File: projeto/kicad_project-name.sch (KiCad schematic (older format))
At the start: 26 parts, among them J1 USB_C_Receptacle_USB2.0, J2 Conn_01x04_Female, Q1 MMBT3904, Q2 MMBT3904, SW1 SW_Push, SW2 SW_Push, U1 TLV75733PDBV, U2 CH340G, U3 ESP32-WROOM-32D, Y1 12MHz 10ppm

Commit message: Troca do LDO para AMS1117-3-3
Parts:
- removed R1: 10kR, Resistor_SMD:R_0603_1608Metric, symbol Device:R_US
- removed SW2: SW_Push, Switches:TACTILE_SWITCH_SMD_6.0X3.5MM, symbol Switch:SW_Push
- removed U1: TLV75733PDBV, Package_TO_SOT_SMD:SOT-23-5, symbol Regulator_Linear:TLV75733PDBV
- added C? (x4): 100nF, Capacitor_SMD:C_0603_1608Metric, symbol Device:C_Small
- added C?: 10nF, Capacitor_SMD:C_0603_1608Metric, symbol Device:C_Small
- added C?: 10uF, Capacitor_Tantalum_SMD:CP_EIA-3216-12_Kemet-S, symbol Device:CP1_Small
- added J?: JTAG 10pin Connector, Connector_PinHeader_1.27mm:PinHeader_2x05_P1.27mm_Vertical_SMD, symbol Connector:Conn_ARM_JTAG_SWD_10
- added R? (x2): 10kR, Resistor_SMD:R_0603_1608Metric, symbol Device:R_US
- added R? (x2): 5k1R, Resistor_SMD:R_0603_1608Metric, symbol Device:R_US
- added SW?: SW_Push, Switches:TACTILE_SWITCH_SMD_6.0X3.5MM, symbol Switch:SW_Push
- added U?: AMS1117-3.3, Package_TO_SOT_SMD:SOT-223-3_TabPin2, symbol Regulator_Linear:AMS1117-3.3
- C7, C8: value C_Small -> 100nF
- J2: value Conn_01x04_Female -> OLED
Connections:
- net labels added: JTAG_RST, MTCK, MTDI, MTDO, MTMS
- net labels removed: 3V3_EN
- wire segments 89 -> 143
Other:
- note added: "Conector Debug/JTAG"
- note added: "OLED"
- note added: "Reset e Boot"
- moved on the sheet: C1, C2, C3, C4, C5, C6, C7, C8, D1, J1, J2, Q1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

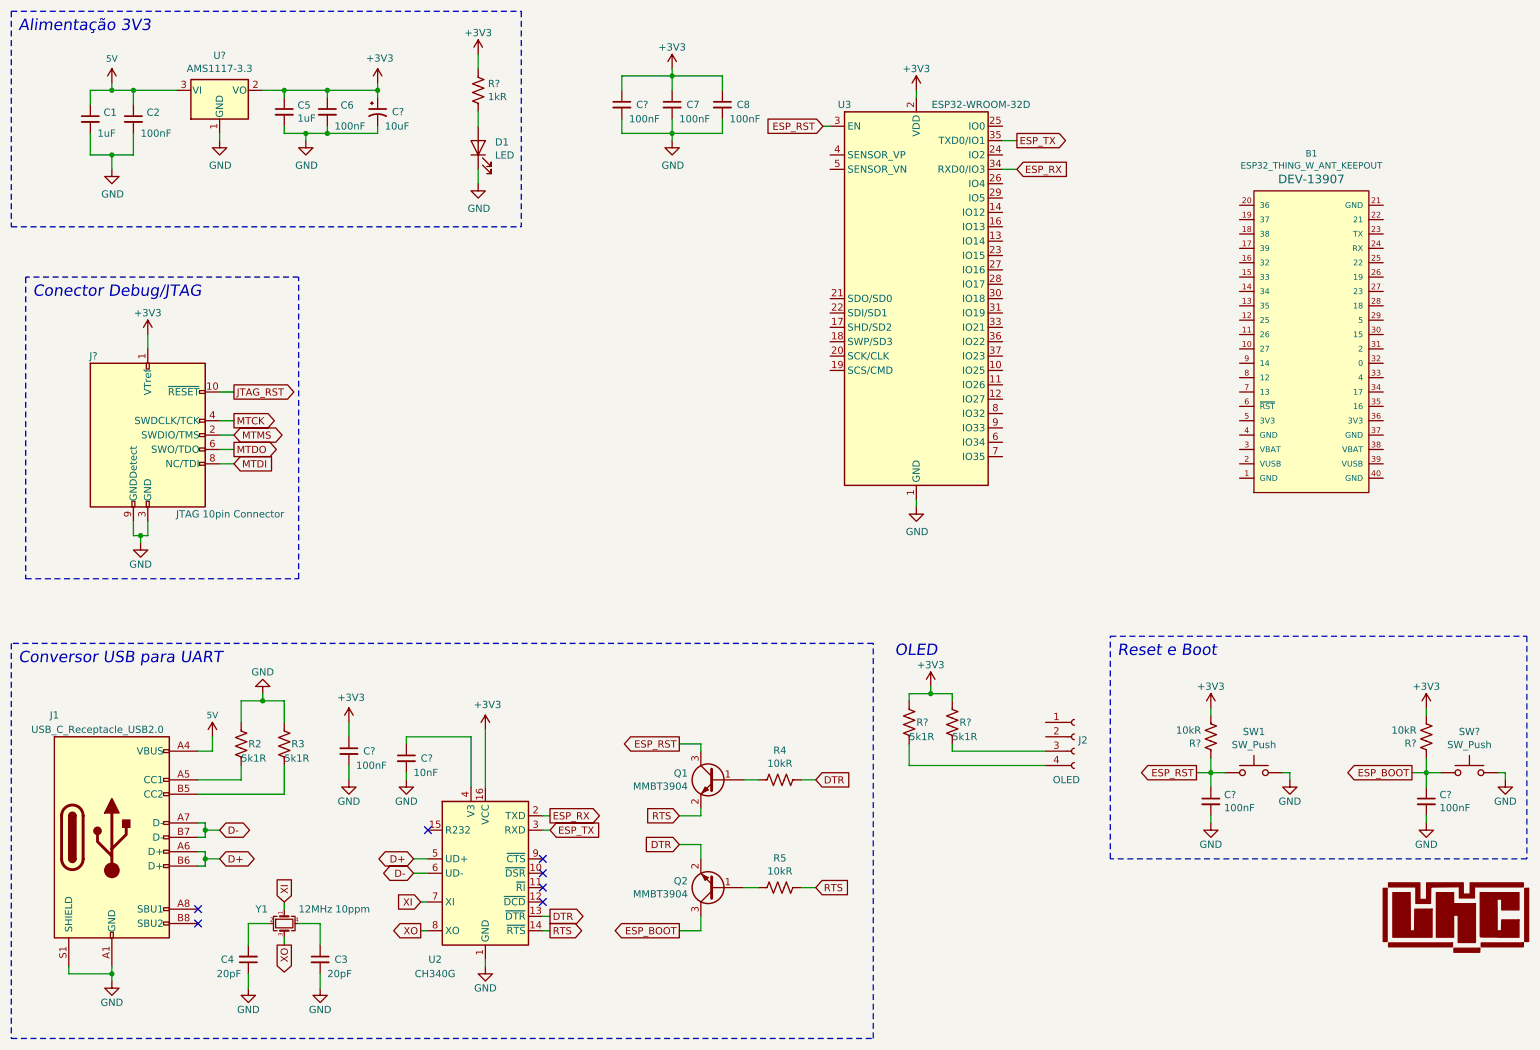
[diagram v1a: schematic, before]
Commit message: Botão de reset/boot e conector OLED
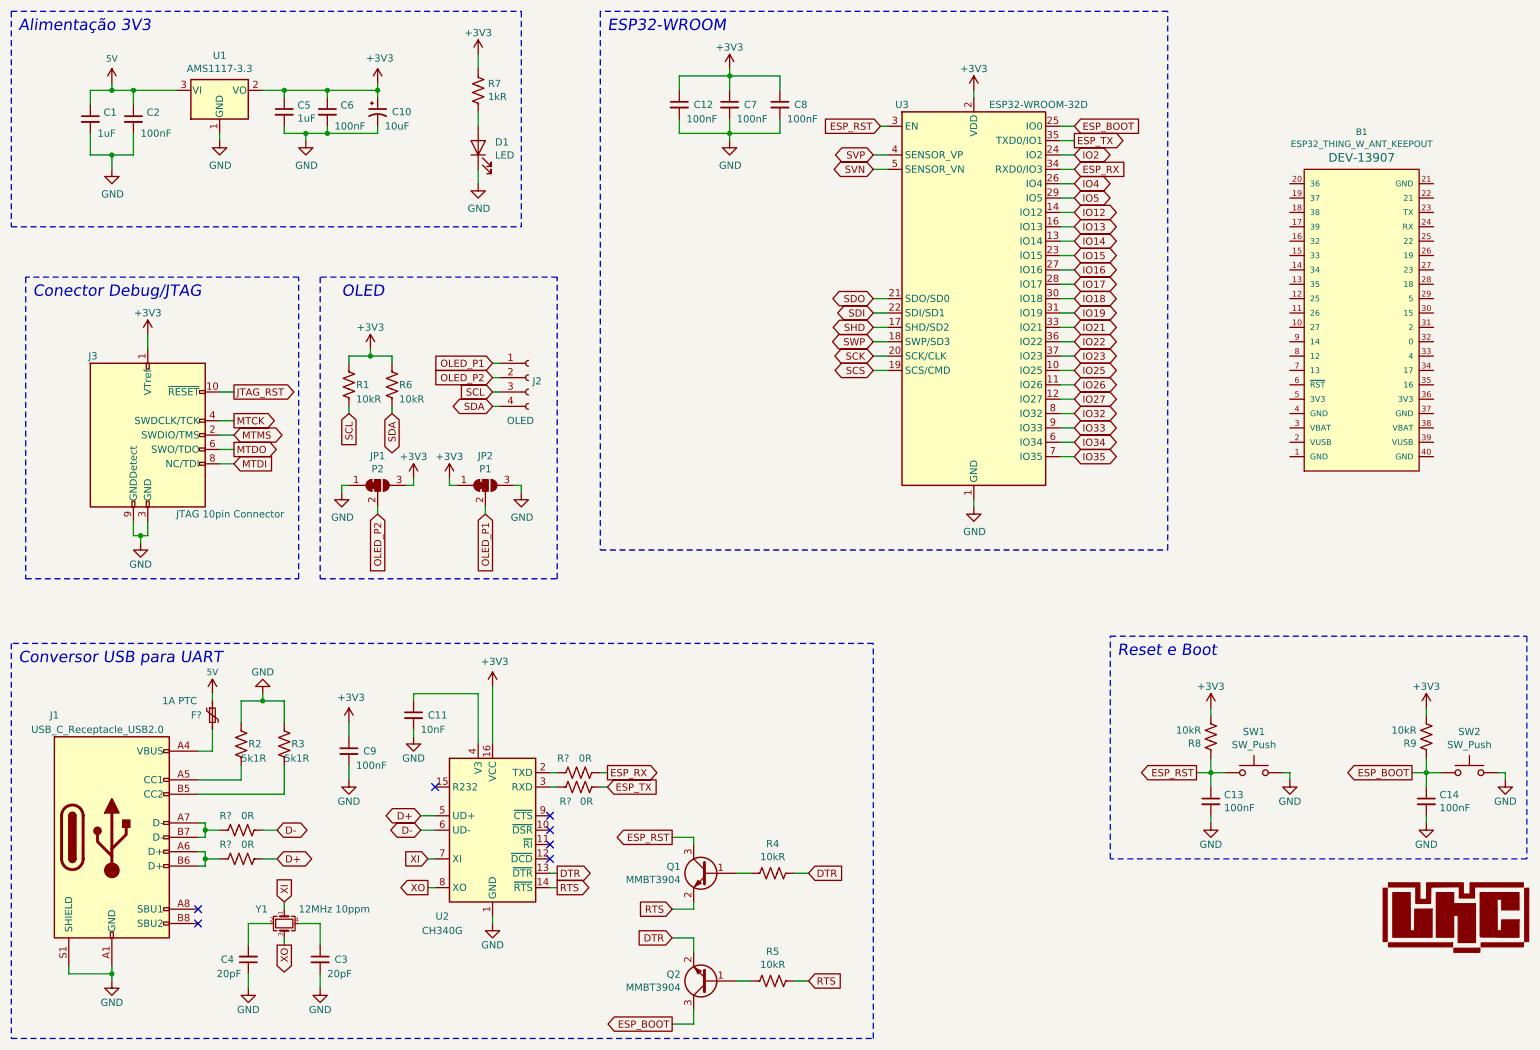
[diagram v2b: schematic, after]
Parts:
- added F?: 1A PTC, Resistor_SMD:R_1210_3225Metric, symbol Device:Polyfuse_Small
- added JP1: P2, Jumper:SolderJumper-3_P1.3mm_Bridged12_Pad1.0x1.5mm_NumberLabels, symbol Jumper:SolderJumper_3_Bridged12
- added JP2: P1, Jumper:SolderJumper-3_P1.3mm_Bridged12_Pad1.0x1.5mm_NumberLabels, symbol Jumper:SolderJumper_3_Bridged12
- added R? (x4): 0R, Resistor_SMD:R_0603_1608Metric, symbol Device:R_US
- R1, R6: renamed from R?; value 5k1R -> 10kR
- gave numbers to parts that had none: 12
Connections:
- net +3V3: now also JP1.3 (B), JP2.1 (A)
- net 5V: now also F?.1; no longer J1.A4 (VBUS), J1.A9 (VBUS), J1.B4 (VBUS), J1.B9 (VBUS)
- net D+: now also R?.1; no longer J1.A6 (D+), J1.B6 (D+)
- net D-: now also R?.1; no longer J1.A7 (D-), J1.B7 (D-)
- net ESP_BOOT: now also U3.25 (IO0)
- net ESP_RX: now also R?.1; no longer U2.2 (TXD)
- net ESP_TX: now also R?.2; no longer U2.3 (RXD)
- net GND: now also JP1.1 (A), JP2.3 (B)
- net IO25: now reaches U3.10 (IO25)
- net IO26: now reaches U3.11 (IO26)
- net IO27: now reaches U3.12 (IO27)
- net IO14: now reaches U3.13 (IO14)
- net IO12: now reaches U3.14 (IO12)
- net IO13: now reaches U3.16 (IO13)
- net SHD: now reaches U3.17 (SHD/SD2)
- net SWP: now reaches U3.18 (SWP/SD3)
- net SCS: now reaches U3.19 (SCS/CMD)
- net SCK: now reaches U3.20 (SCK/CLK)
- net SDO: now reaches U3.21 (SDO/SD0)
- net SDI: now reaches U3.22 (SDI/SD1)
- net IO15: now reaches U3.23 (IO15)
- net IO2: now reaches U3.24 (IO2)
- net IO4: now reaches U3.26 (IO4)
- net IO16: now reaches U3.27 (IO16)
- net IO17: now reaches U3.28 (IO17)
- net IO5: now reaches U3.29 (IO5)
- net IO18: now reaches U3.30 (IO18)
- net IO19: now reaches U3.31 (IO19)
- net IO21: now reaches U3.33 (IO21)
- net IO22: now reaches U3.36 (IO22)
- net IO23: now reaches U3.37 (IO23)
- net SVP: now reaches U3.4 (SENSOR_VP)
- net SVN: now reaches U3.5 (SENSOR_VN)
- net IO34: now reaches U3.6 (IO34)
- net IO35: now reaches U3.7 (IO35)
- net IO32: now reaches U3.8 (IO32)
- net IO33: now reaches U3.9 (IO33)
- net OLED_P1: now reaches J2.1 (Pin_1)
- net OLED_P1: now also JP2.2 (C)
- net OLED_P2: now reaches J2.2 (Pin_2)
- net OLED_P2: now also JP1.2 (C)
- net SCL: now reaches J2.3 (Pin_3)
- net SCL: now also R1.2; no longer R6.2
- net SDA: now reaches J2.4 (Pin_4)
- net SDA: now also R6.2; no longer R1.2
- new net: F?.2, J1.A4 (VBUS), J1.A9 (VBUS), J1.B4 (VBUS), J1.B9 (VBUS)
- new net: J1.A6 (D+), J1.B6 (D+), R?.2
- new net: J1.A7 (D-), J1.B7 (D-), R?.2
- new net: R?.2, U2.2 (TXD)
- new net: R?.1, U2.3 (RXD)
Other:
- note added: "ESP32-WROOM"
- moved on the sheet: B1, C11, C12, C7, C8, J2, Q1, Q2, R1, R4, R5, R6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
